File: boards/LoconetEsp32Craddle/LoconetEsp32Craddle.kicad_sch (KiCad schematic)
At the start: 29 parts, among them J1 SD1306 I2C/Oled, Q3 2N7002, Q4 2N7002, Q5 2N7002, SW1 SW_Push, SW2 SW_Push, U5 ESP32-DevKitC

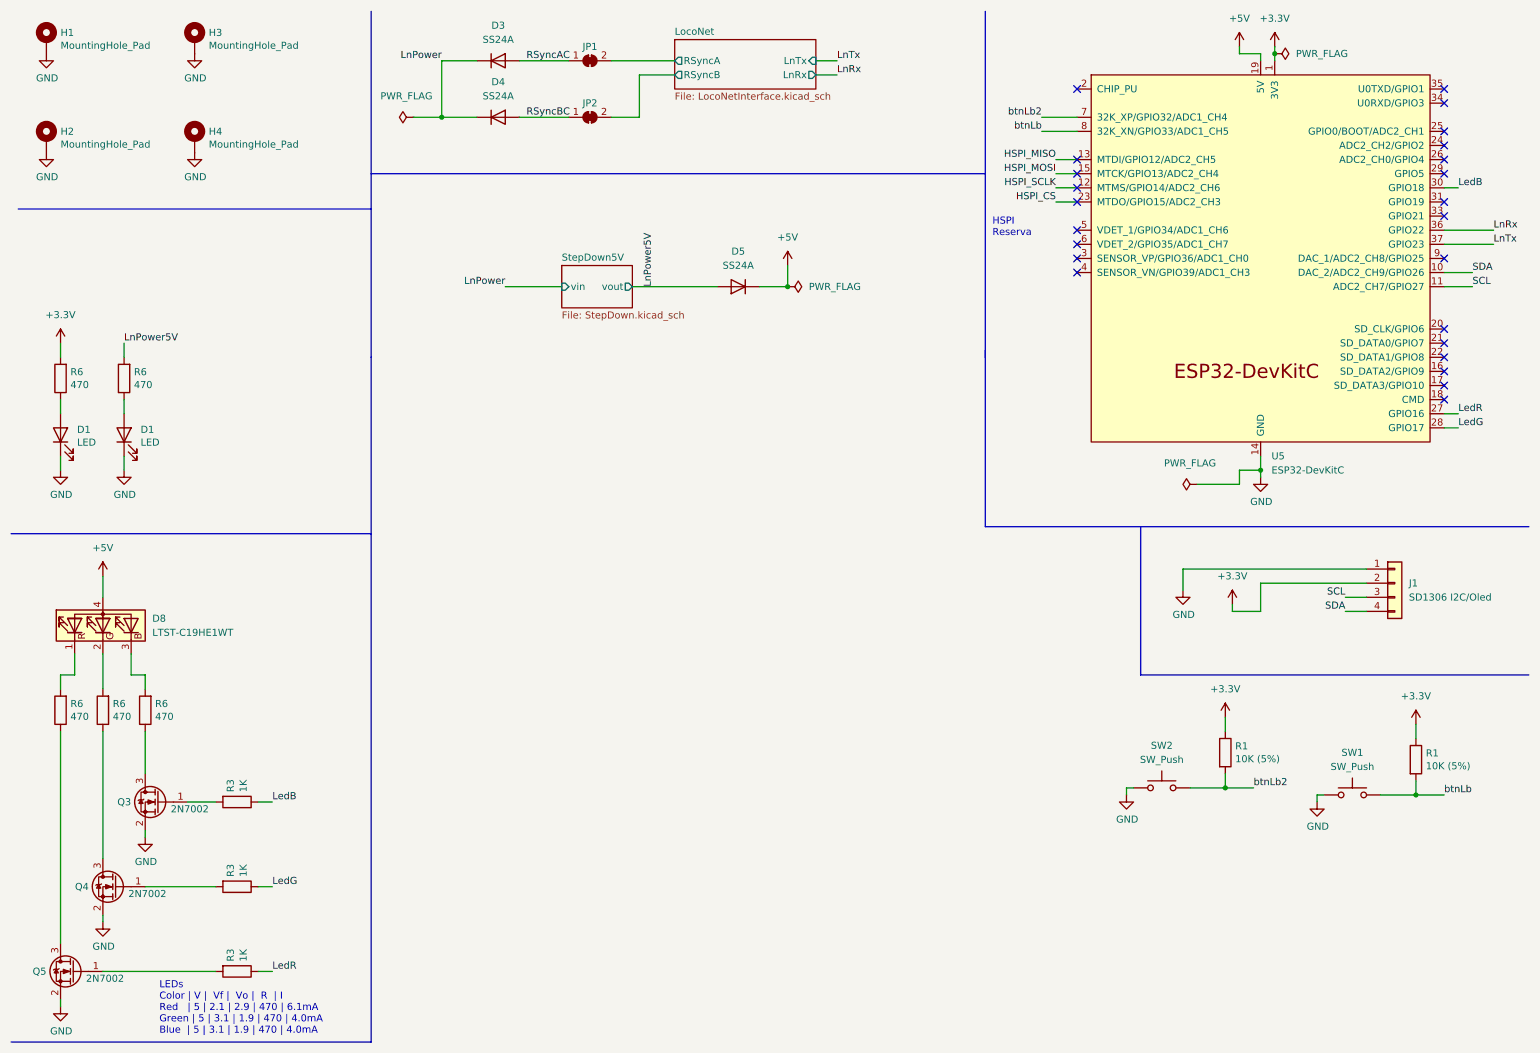
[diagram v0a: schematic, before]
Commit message: Update a Kicad 10 y eliminacion ERC
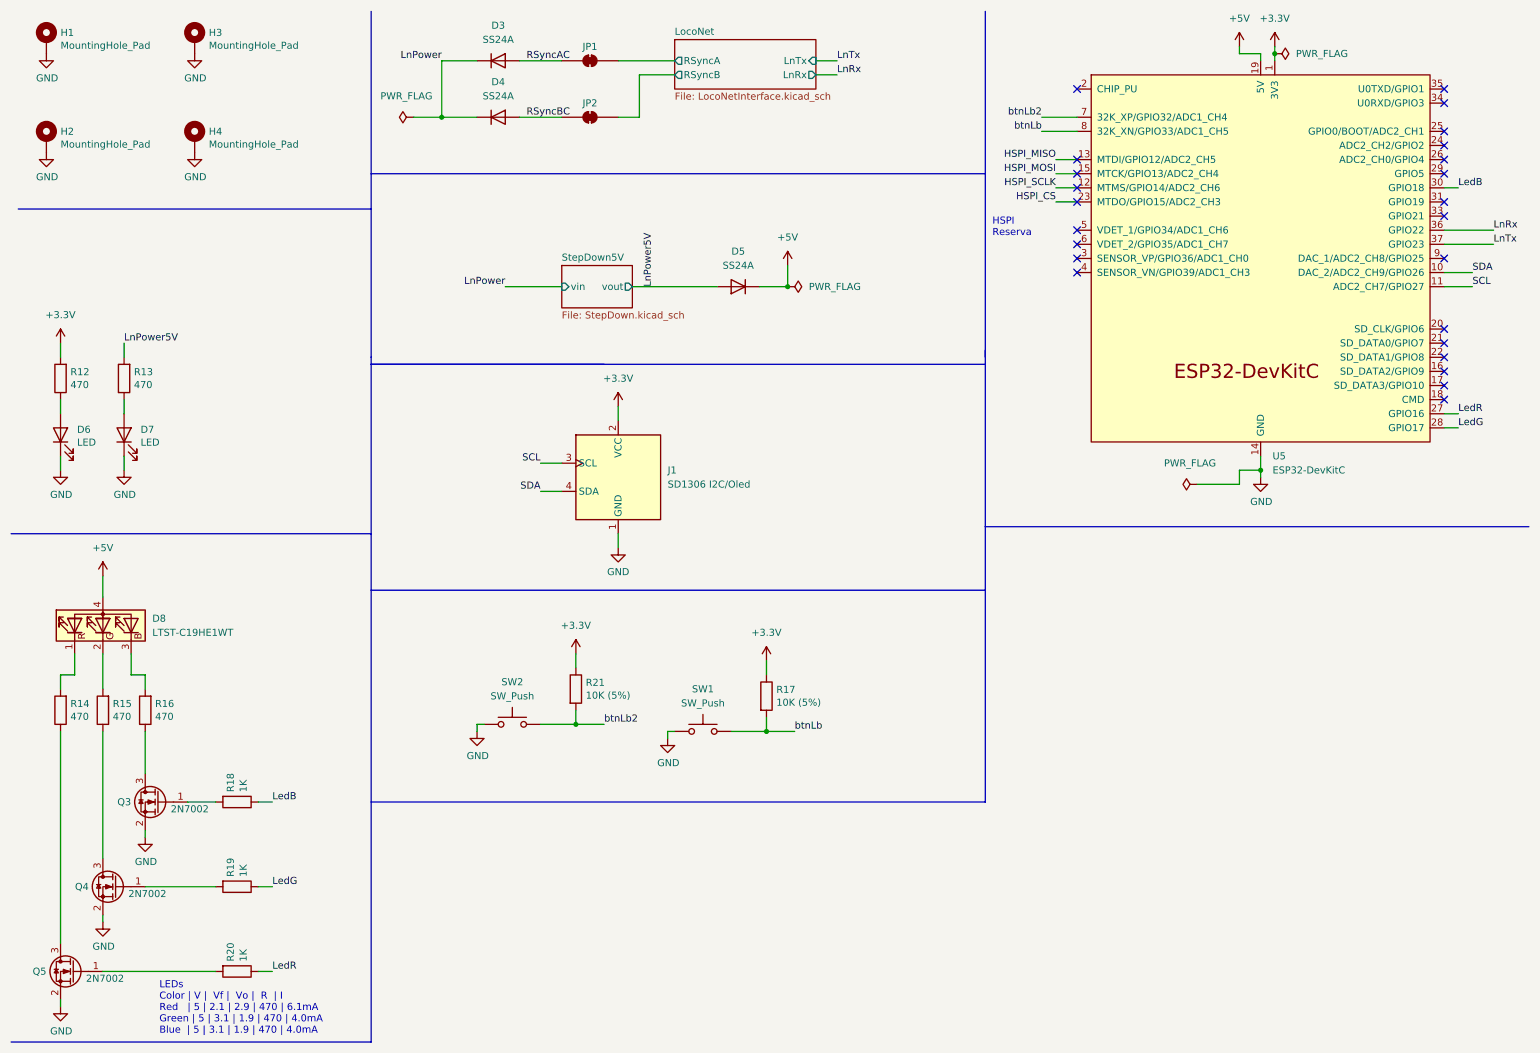
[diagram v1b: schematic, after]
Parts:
- J1: footprint LocoNetInterface:128x64OLED -> LocoNetInterface:ER_OLEDM0.91_1x-I2C-128x64OLED; symbol Connector_Generic:Conn_01x04 -> Display_Graphic:ER_OLEDM0.91_1x-I2C
- U5: footprint Espressif:ESP32-DevKitC -> PCM_Espressif:ESP32-DevKitC
- renumbered D1 to D6, D1 to D7, R6 to R12, R6 to R13, R6 to R14, R6 to R15, R6 to R16, R1 to R17, R3 to R18, R3 to R19, R3 to R20, R1 to R21
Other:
- moved on the sheet: R17, R21, SW1, SW2
